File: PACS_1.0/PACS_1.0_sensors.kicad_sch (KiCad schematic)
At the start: 0 parts

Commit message: Added Bucks, Temp and Light Sensor
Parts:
- added C16: 1uF, symbol Device:C
- added U4: LTR-303ALS-01, OptoDevice:Lite-On_LTR-303ALS-01, symbol Sensor_Optical:LTR-303ALS-01
- added U5: MCP9700Ax-ETT, Package_TO_SOT_SMD:SOT-23, symbol Sensor_Temperature:MCP9700Ax-ETT
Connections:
- new net +3.3V: C16.2, U4.1 (VDD), U5.1 (V_{DD})
- new net Analog_0: U5.2 (V_{OUT})
- new net GND: C16.1, U4.3 (GND), U5.3 (GND)
- new net SCL: U4.4 (SCL)
- new net SDA: U4.6 (SDA)
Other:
- note added: "Ambient Light Sensor"
- note added: "Temperature Sensor"

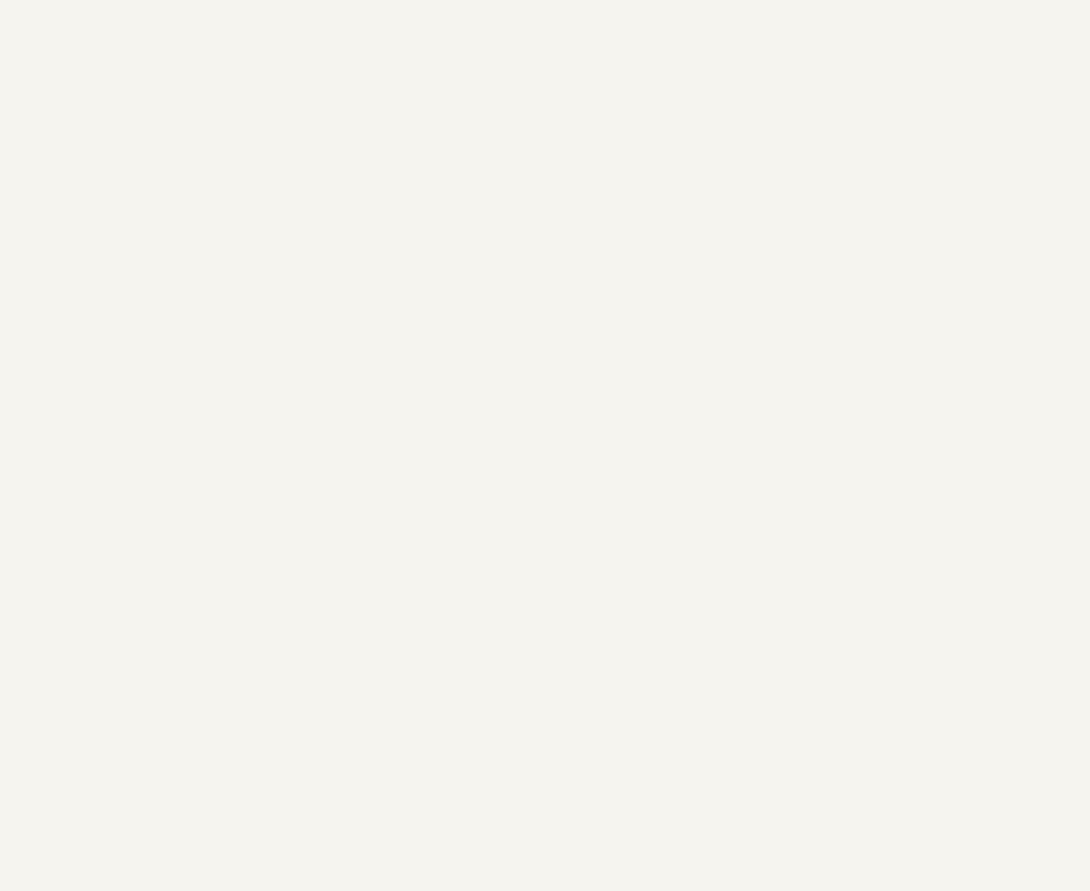
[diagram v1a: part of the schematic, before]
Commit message: New Changes
We had the discussion about water pump, INA, LEDS, and battery solution. Not much changes from previous night.
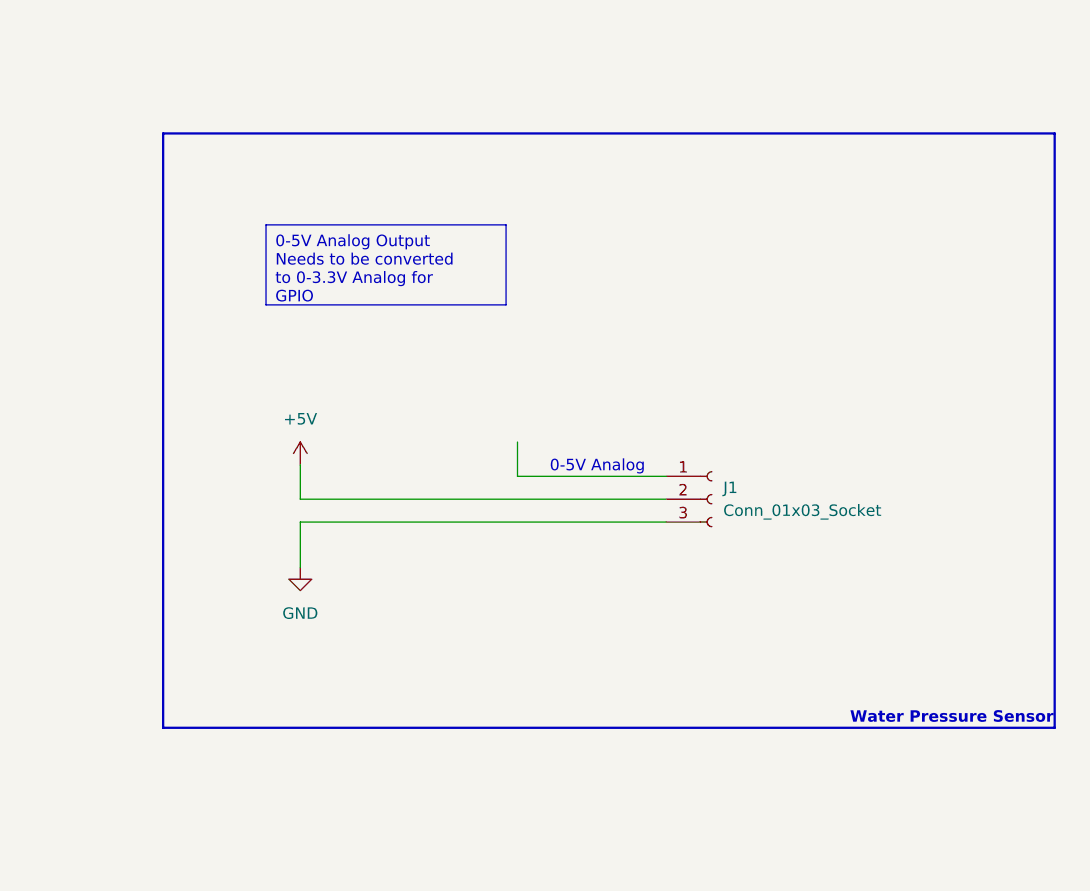
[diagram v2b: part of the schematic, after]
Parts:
- added J1: Conn_01x03_Socket, symbol Connector:Conn_01x03_Socket
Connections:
- net GND: now also J1.3 (Pin_3)
- new net +5V: J1.2 (Pin_2)
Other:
- note added: "0-5V Analog"
- note added: "Water Pressure Sensor"

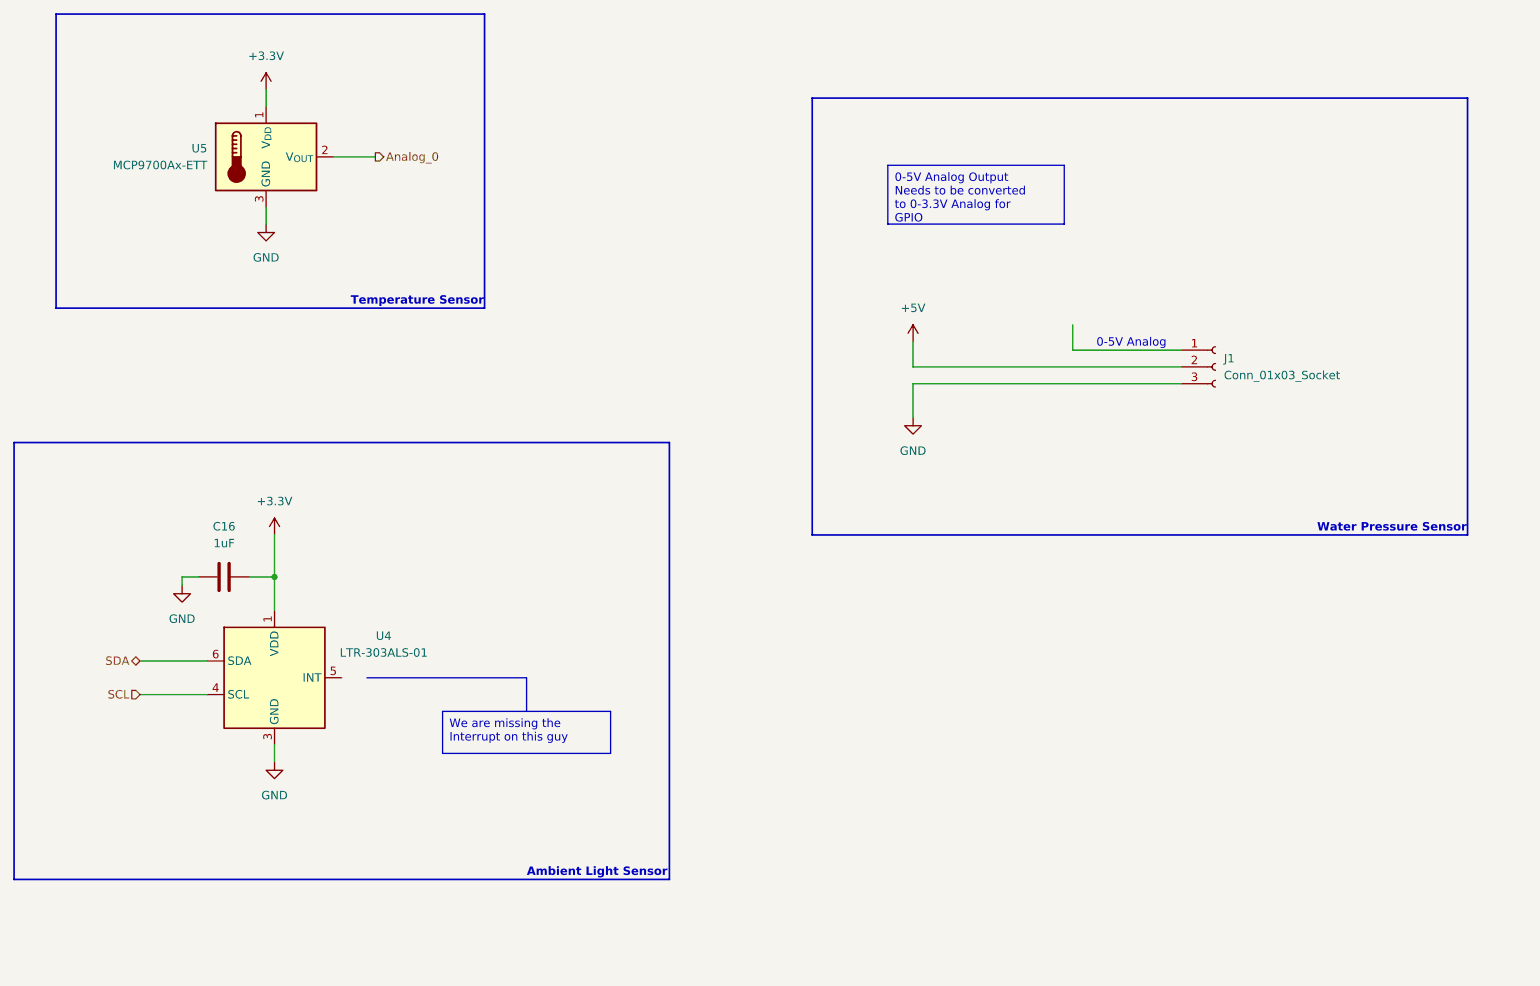
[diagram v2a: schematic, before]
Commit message: Added Water level sensor and start of Pump
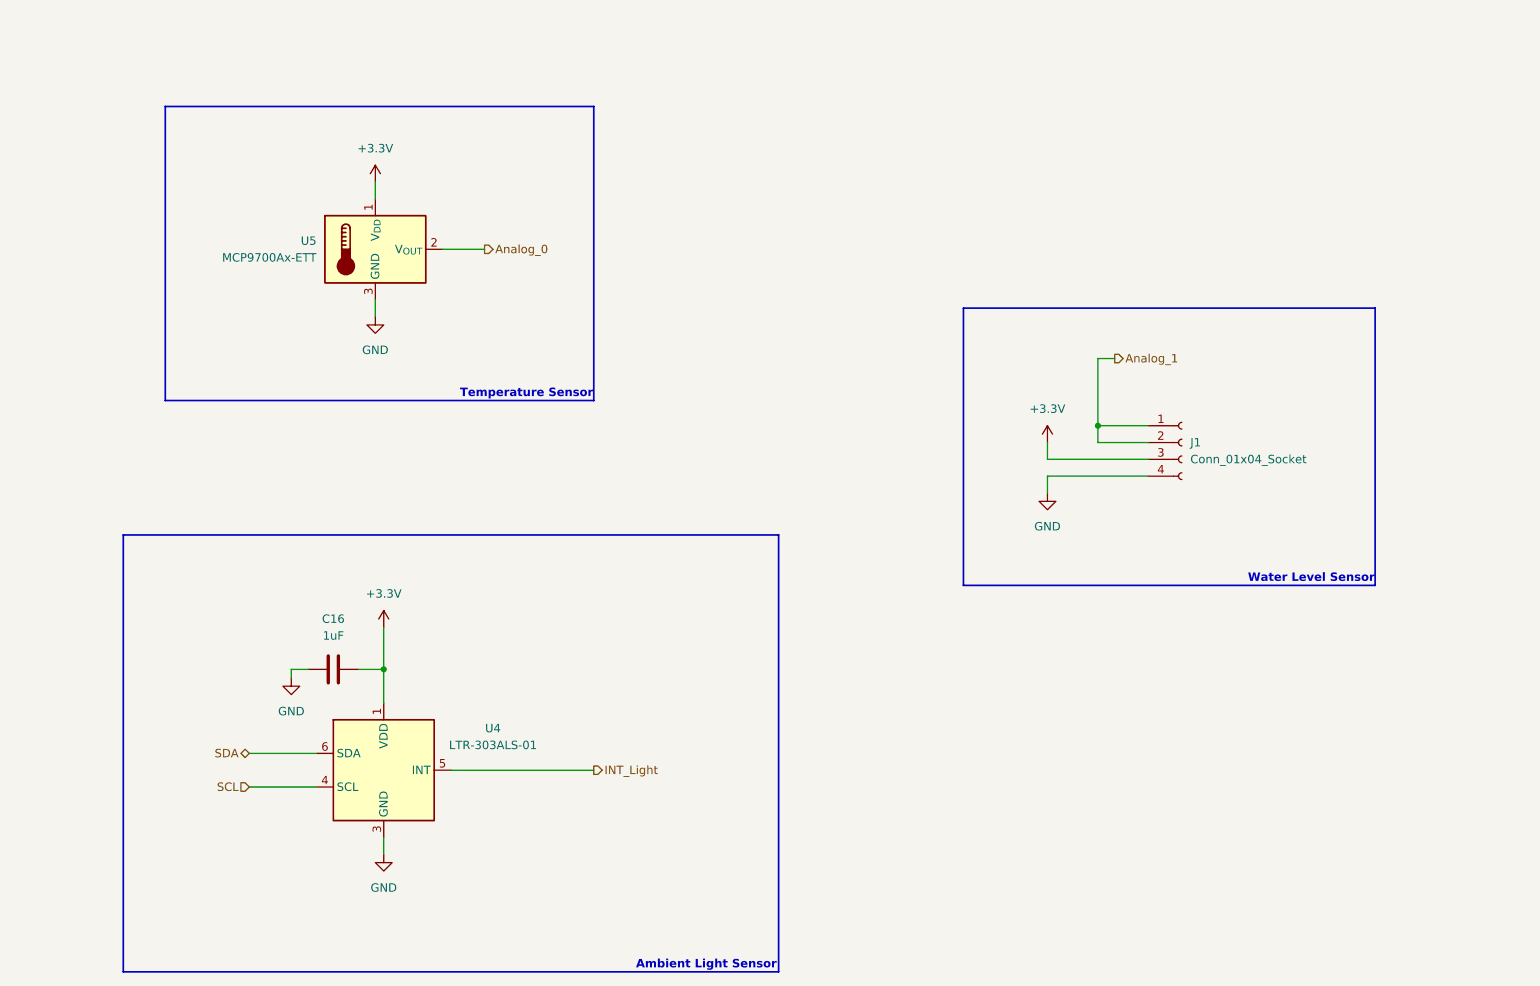
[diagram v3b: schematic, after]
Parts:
- removed J1: Conn_01x03_Socket, symbol Connector:Conn_01x03_Socket
- added J1: Conn_01x04_Socket, symbol Connector:Conn_01x04_Socket
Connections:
- net +3.3V: now also J1.3 (Pin_3)
- net GND: now also J1.4 (Pin_4)
- net INT_Light: now reaches U4.5 (INT)
- new net Analog_1: J1.1 (Pin_1), J1.2 (Pin_2)
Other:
- note added: "Water Level Sensor"
- note removed: "0-5V Analog"
- note removed: "Water Pressure Sensor"
- moved on the sheet: C16, U4, U5

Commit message: Finished water pump, cleaned out empty sheets, added details in 'post its'
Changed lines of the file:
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@@
 	(rectangle
 		(start 184.15 64.77)
-		(end 246.38 106.68)
+		(end 267.97 106.68)
 		(stroke
 			(width 0.254)
@@
 		)
 	)
+	(text_box "Header for the Water Level Sensor. Outside pins (1 and 4) are the reference resistor Rref, and innner pins (2 and 3) are the sensor output Rsense."
+		(exclude_from_sim no)
+		(at 228.6 67.31 0)
+		(size 34.29 12.7)
+		(stroke
+			(width 0)
+			(type default)
+		)
+		(fill
+			(type color)
+			(color 255 255 194 1)
+		)
+		(effects
+			(font
+				(size 1.27 1.27)
+				(color 0 0 0 1)
+			)
+			(justify left top)
+		)
+	)
 	(text "Water Level Sensor\n"
 		(exclude_from_sim no)
-		(at 236.728 105.664 0)
+		(at 257.81 105.664 0)
 		(effects
 			(font

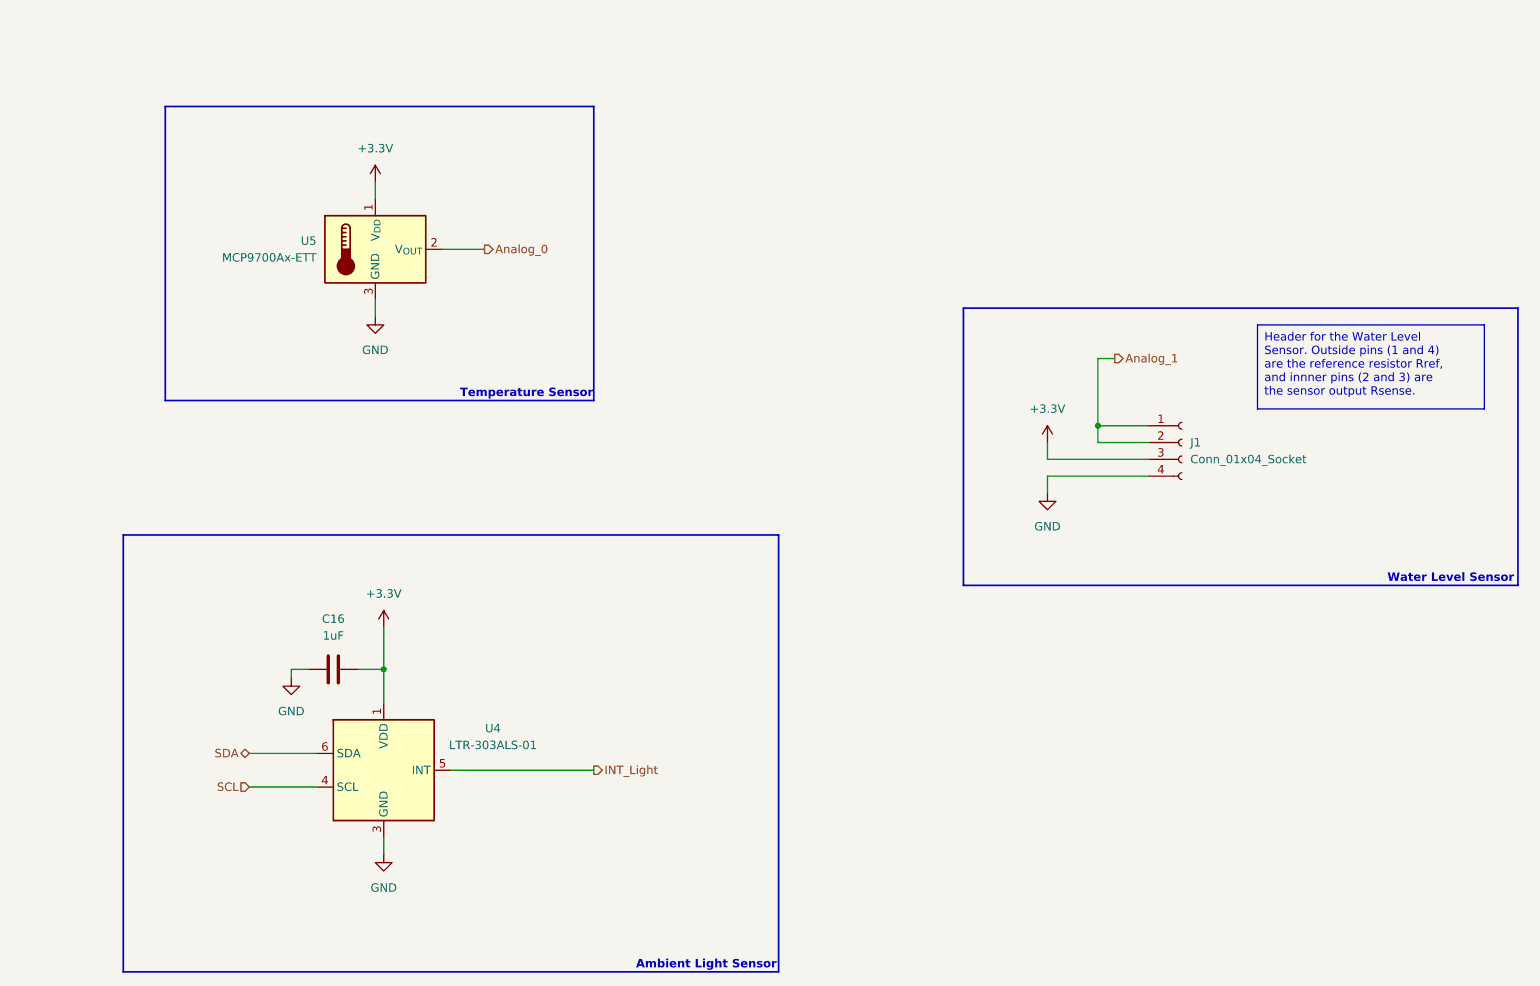
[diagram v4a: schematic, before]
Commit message: Finished 1.0 (NO INA INCLUDED)
Finished PACS 1.0 sheets, Power sheet needs considerations, no INA yet.
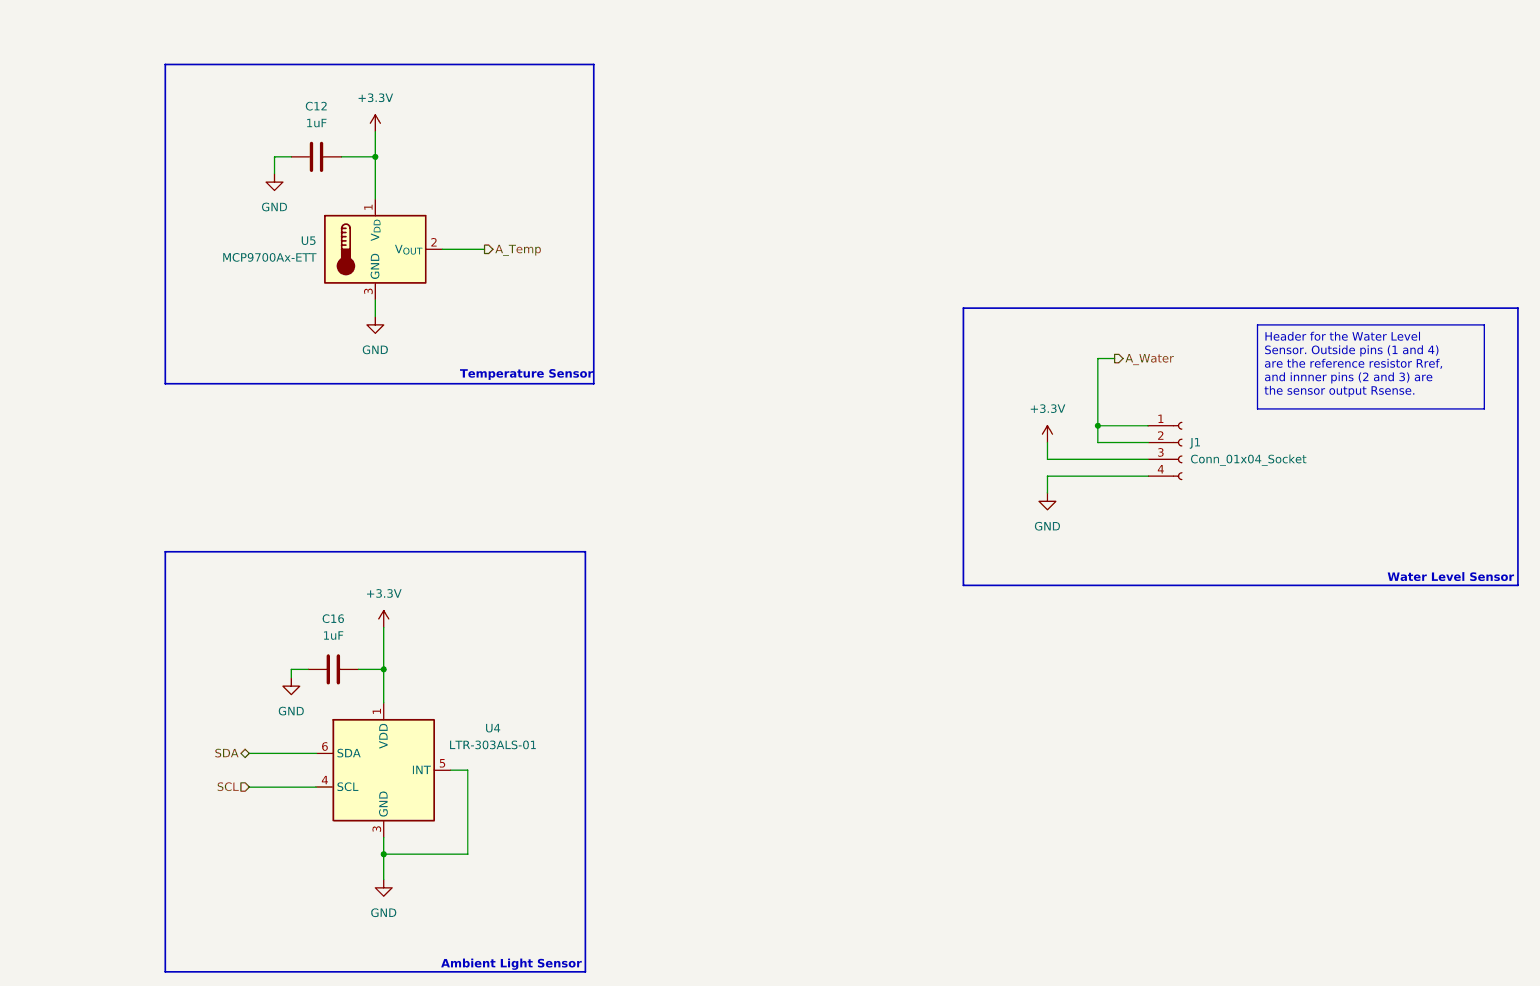
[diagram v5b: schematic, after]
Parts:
- added C12: 1uF, symbol Device:C
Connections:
- net INT_Light is gone; now on net GND: U4.5 (INT)
- net +3.3V: now also C12.2
- net GND: now also C12.1
- net Analog_0 renamed A_Temp
- net Analog_1 renamed A_Water
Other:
- title: (none) -> Sensors
